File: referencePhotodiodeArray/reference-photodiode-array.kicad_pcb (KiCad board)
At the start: 2 copper layers, 28 x 28 mm, 18 parts

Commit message: diode substrate design "done"
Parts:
- added G***: value, testPad:logo_small, F.Cu at (24.5, -14.0)
- moved D1 1.96 mm to (6.97, -16.7)
- moved D8 1.96 mm to (21.0, -11.3)
- moved D5 1.68 mm to (16.3, -16.7)
- moved D4 1.68 mm to (11.7, -11.3)
- moved D2 1.52 mm to (6.98, -9.73)
- moved D7 1.50 mm to (21.0, -18.3)
- moved D3 1.20 mm to (11.7, -18.3)
- moved D6 1.20 mm to (16.3, -9.74)
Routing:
- net /com: track 56.6 -> 0.00 mm
- net Net-(D8-Pad2): track 4.04 -> 5.95 mm
- net Net-(D1-Pad2): track 4.04 -> 5.95 mm
- net Net-(D4-Pad2): track 3.50 -> 5.20 mm
- net Net-(D5-Pad2): track 3.50 -> 5.20 mm
- added copper zone on B.Cu, net /com
- added copper zone on F.Cu, net /com
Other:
- board text added: "v1.00"

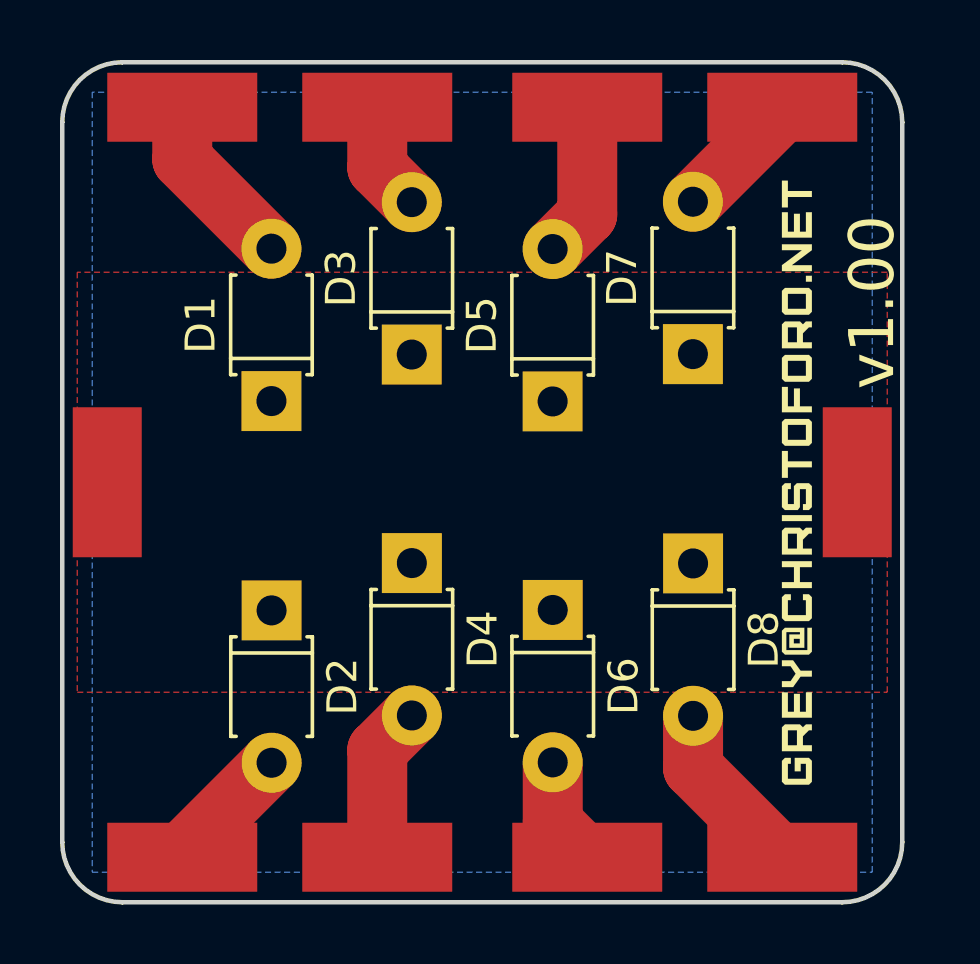
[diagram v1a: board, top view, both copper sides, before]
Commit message: fix reference photodiode array
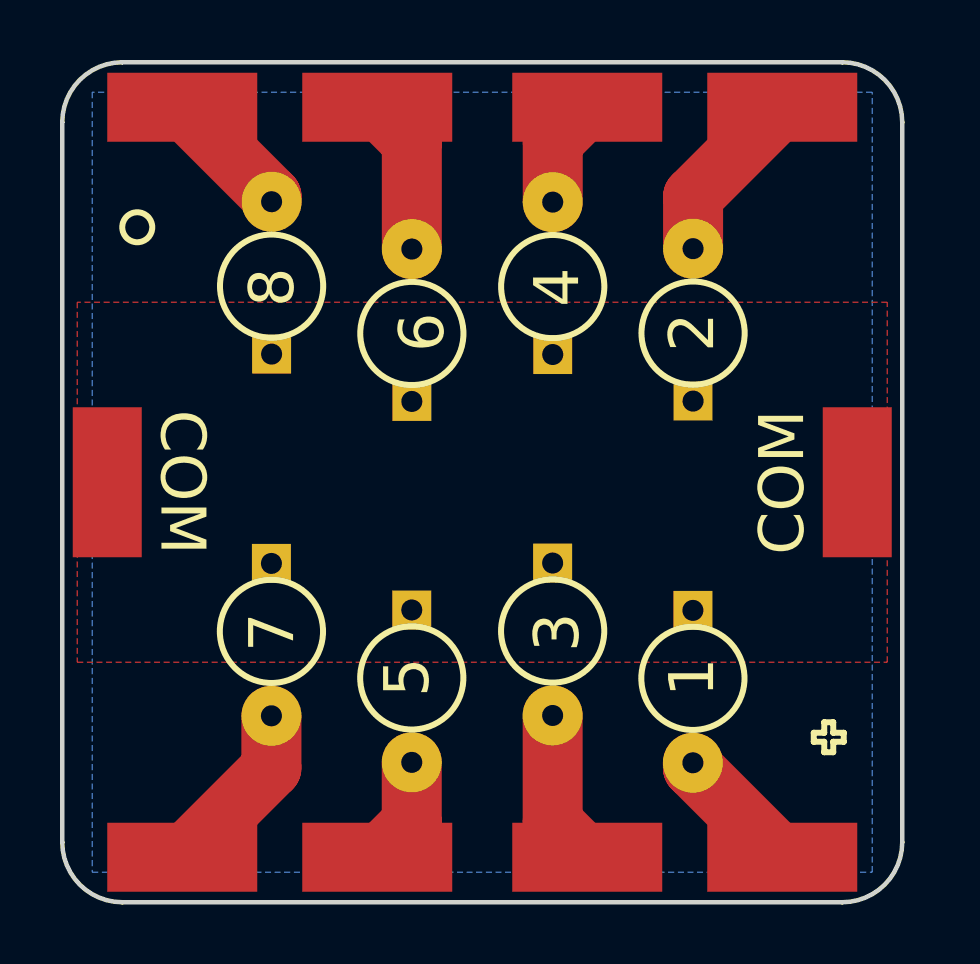
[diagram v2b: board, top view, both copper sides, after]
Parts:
- D1, D2, D3, D4, D5, D6, D7, D8: footprint Diodes_ThroughHole:D_T-1_P5.08mm_Horizontal -> testPad:BPW34; moved to B.Cu
- G***: moved to B.Cu
- moved G*** 2.50 mm to (27.0, -14.0), turned to 270 degrees
- moved D1 1.57 mm to (6.98, -18.3)
- moved D8 1.57 mm to (21.0, -9.73)
- moved D2 1.57 mm to (6.97, -11.3)
- moved D7 1.57 mm to (21.0, -16.7)
- moved D3 1.56 mm to (11.7, -16.7)
- moved D6 1.56 mm to (16.3, -11.3)
- moved D5 1.56 mm to (16.3, -18.3)
- moved D4 1.56 mm to (11.7, -9.74)
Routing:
- net Net-(D6-Pad2): track 3.64 -> 5.20 mm
- net Net-(D3-Pad2): track 3.64 -> 5.20 mm
- net Net-(D4-Pad2): track 5.20 -> 3.64 mm
- net Net-(D5-Pad2): track 5.20 -> 3.64 mm
- net Net-(D8-Pad2): track 5.95 -> 4.38 mm
- net Net-(D1-Pad2): track 5.95 -> 4.38 mm
- net Net-(D2-Pad2): track 4.38 -> 5.95 mm
- net Net-(D7-Pad2): track 4.38 -> 5.95 mm
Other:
- board text added: "1"
- board text added: "2"
- board text added: "3"
- board text added: "4"
- board text added: "5"
- board text added: "6"
- board text added: "7"
- board text added: "8"
- board text added: "COM"
- board text added: "v1.01"
- board text removed: "v1.00"
